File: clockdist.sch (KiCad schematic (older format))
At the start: 6 parts, among them U33 74LS258

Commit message: Fix some symbols
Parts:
- gave numbers to parts that had none: 1
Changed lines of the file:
@@
 U 1 1 5D89015C
 P 4050 2800
-F 0 "U33" H 4075 3125 50  0000 C CNN
-F 1 "74LS258" H 4075 3034 50  0000 C CNN
+F 0 "U33" H 4100 2950 50  0000 C CNN
+F 1 "74LS258" H 3750 2600 50  0000 C CNN
 F 2 "" H 4050 2800 50  0001 C CNN
 F 3 "http://www.ti.com/lit/gpn/sn74LS258" H 4050 2800 50  0001 C CNN
@@
 CCK
 $Comp
-L 74ls258:74LS258 U?
+L 74ls258:74LS258 U33
 U 2 1 5D895568
 P 4050 4200
-F 0 "U?" H 4075 4525 50  0000 C CNN
-F 1 "74LS258" H 4075 4434 50  0000 C CNN
+F 0 "U33" H 4100 4350 50  0000 C CNN
+F 1 "74LS258" H 3750 4000 50  0000 C CNN
 F 2 "" H 7150 1900 50  0001 C CNN
 F 3 "http://www.ti.com/lit/gpn/sn74LS258" H 7150 1900 50  0001 C CNN
@@
 $EndComp
 $Comp
-L 74ls258:74LS258 U?
+L 74ls258:74LS258 U33
 U 3 1 5D8955FE
 P 4050 3500
-F 0 "U?" H 4075 3825 50  0000 C CNN
-F 1 "74LS258" H 4075 3734 50  0000 C CNN
+F 0 "U33" H 4100 3650 50  0000 C CNN
+F 1 "74LS258" H 3750 3300 50  0000 C CNN
 F 2 "" H 7150 1200 50  0001 C CNN
 F 3 "http://www.ti.com/lit/gpn/sn74LS258" H 7150 1200 50  0001 C CNN
@@
 $EndComp
 $Comp
-L power:GND #PWR?
+L power:GND #PWR0202
 U 1 1 5D8A9F76
 P 8950 4200
-F 0 "#PWR?" H 8950 3950 50  0001 C CNN
+F 0 "#PWR0202" H 8950 3950 50  0001 C CNN
 F 1 "GND" H 8955 4027 50  0000 C CNN
 F 2 "" H 8950 4200 50  0001 C CNN
@@
 	8950 4200 8950 4050
 $Comp
-L power:VCC #PWR?
+L power:VCC #PWR0203
 U 1 1 5D8AA81C
 P 8950 2950
-F 0 "#PWR?" H 8950 2800 50  0001 C CNN
+F 0 "#PWR0203" H 8950 2800 50  0001 C CNN
 F 1 "VCC" H 8967 3123 50  0000 C CNN
 F 2 "" H 8950 2950 50  0001 C CNN
@@
 	4700 3000 4700 3700
 $Comp
-L power:GND #PWR?
+L power:GND #PWR0204
 U 1 1 5D8ABB37
 P 4700 4850
-F 0 "#PWR?" H 4700 4600 50  0001 C CNN
+F 0 "#PWR0204" H 4700 4600 50  0001 C CNN
 F 1 "GND" H 4705 4677 50  0000 C CNN
 F 2 "" H 4700 4850 50  0001 C CNN

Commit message: Add video power
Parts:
- RP103: footprint (none) -> Resistor_THT:R_Array_SIP10
- U33: footprint (none) -> Package_DIP:DIP-16_W7.62mm_Socket_LongPads
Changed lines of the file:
@@
 F 0 "U33" H 4100 2950 50  0000 C CNN
 F 1 "74LS258" H 3750 2600 50  0000 C CNN
-F 2 "" H 4050 2800 50  0001 C CNN
+F 2 "Package_DIP:DIP-16_W7.62mm_Socket_LongPads" H 4050 2800 50  0001 C CNN
 F 3 "http://www.ti.com/lit/gpn/sn74LS258" H 4050 2800 50  0001 C CNN
 	1    4050 2800
@@
 F 0 "U33" H 4100 4350 50  0000 C CNN
 F 1 "74LS258" H 3750 4000 50  0000 C CNN
-F 2 "" H 7150 1900 50  0001 C CNN
+F 2 "Package_DIP:DIP-16_W7.62mm_Socket_LongPads" H 7150 1900 50  0001 C CNN
 F 3 "http://www.ti.com/lit/gpn/sn74LS258" H 7150 1900 50  0001 C CNN
 	2    4050 4200
@@
 F 0 "U33" H 4100 3650 50  0000 C CNN
 F 1 "74LS258" H 3750 3300 50  0000 C CNN
-F 2 "" H 7150 1200 50  0001 C CNN
+F 2 "Package_DIP:DIP-16_W7.62mm_Socket_LongPads" H 7150 1200 50  0001 C CNN
 F 3 "http://www.ti.com/lit/gpn/sn74LS258" H 7150 1200 50  0001 C CNN
 	3    4050 3500
@@
 F 0 "RP103" V 5233 3500 50  0000 C CNN
 F 1 "39" V 5324 3500 50  0000 C CNN
-F 2 "" V 6025 3500 50  0001 C CNN
+F 2 "Resistor_THT:R_Array_SIP10" V 6025 3500 50  0001 C CNN
 F 3 "~" H 5650 3500 50  0001 C CNN
 	1    5650 3500
@@
 F 0 "U33" H 9180 3671 50  0000 L CNN
 F 1 "74LS258" H 9180 3580 50  0000 L CNN
-F 2 "" H 12050 1300 50  0001 C CNN
+F 2 "Package_DIP:DIP-16_W7.62mm_Socket_LongPads" H 12050 1300 50  0001 C CNN
 F 3 "http://www.ti.com/lit/gpn/sn74LS258" H 12050 1300 50  0001 C CNN
 	5    8950 3600

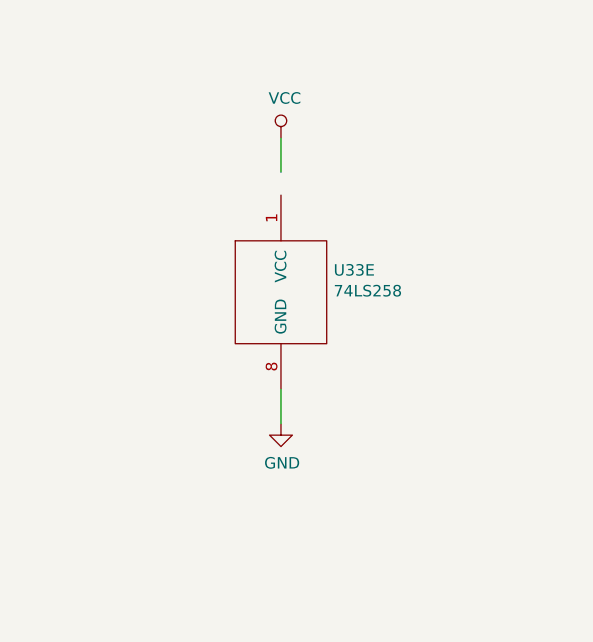
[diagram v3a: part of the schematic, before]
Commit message: Add power & decoupling, not yet complete
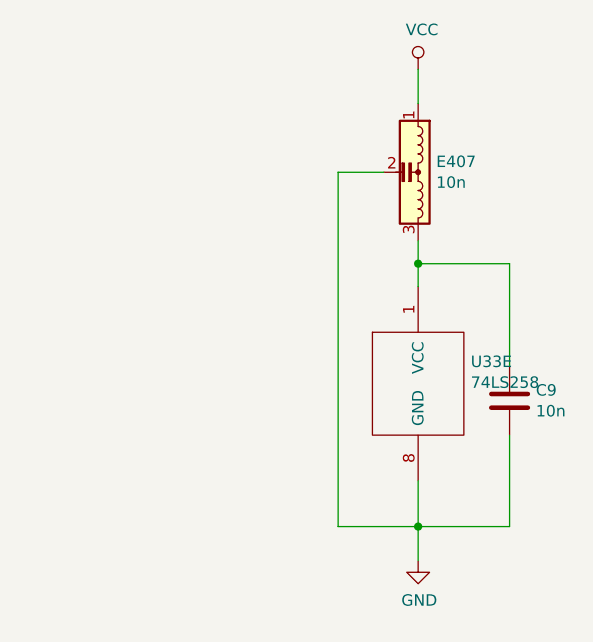
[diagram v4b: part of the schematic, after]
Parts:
- added C9: 10n, symbol Device:C
- added E407: 10n, symbol emi_filter_lcl_small:EMI_Filter_LCL
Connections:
- net GND: now also C9.2, E407.2
- net VCC: now also E407.1
- net at U33.1 (VCC): now also C9.1, E407.3
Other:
- moved on the sheet: U33E
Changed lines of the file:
@@
 $Descr A4 11693 8268
 encoding utf-8
-Sheet 10 11
+Sheet 10 12
 Title "Rämixx500"
 Date "2019-04-20"
@@
 L 74ls258:74LS258 U33
 U 5 1 5D8A9E7D
-P 8950 3600
-F 0 "U33" H 9180 3671 50  0000 L CNN
-F 1 "74LS258" H 9180 3580 50  0000 L CNN
-F 2 "Package_DIP:DIP-16_W7.62mm_Socket_LongPads" H 12050 1300 50  0001 C CNN
-F 3 "http://www.ti.com/lit/gpn/sn74LS258" H 12050 1300 50  0001 C CNN
-	5    8950 3600
+P 9550 4000
+F 0 "U33" H 9780 4071 50  0000 L CNN
+F 1 "74LS258" H 9780 3980 50  0000 L CNN
+F 2 "Package_DIP:DIP-16_W7.62mm_Socket_LongPads" H 12650 1700 50  0001 C CNN
+F 3 "http://www.ti.com/lit/gpn/sn74LS258" H 12650 1700 50  0001 C CNN
+	5    9550 4000
 	1    0    0    -1
 $EndComp
@@
 L power:GND #PWR0202
 U 1 1 5D8A9F76
-P 8950 4200
-F 0 "#PWR0202" H 8950 3950 50  0001 C CNN
-F 1 "GND" H 8955 4027 50  0000 C CNN
-F 2 "" H 8950 4200 50  0001 C CNN
-F 3 "" H 8950 4200 50  0001 C CNN
-	1    8950 4200
-	1    0    0    -1
-$EndComp
-Wire Wire Line
-	8950 4200 8950 4050
+P 9550 4800
+F 0 "#PWR0202" H 9550 4550 50  0001 C CNN
+F 1 "GND" H 9555 4627 50  0000 C CNN
+F 2 "" H 9550 4800 50  0001 C CNN
+F 3 "" H 9550 4800 50  0001 C CNN
+	1    9550 4800
+	1    0    0    -1
+$EndComp
+Wire Wire Line
+	9550 4800 9550 4650
 $Comp
 L power:VCC #PWR0203
 U 1 1 5D8AA81C
-P 8950 2950
-F 0 "#PWR0203" H 8950 2800 50  0001 C CNN
-F 1 "VCC" H 8967 3123 50  0000 C CNN
-F 2 "" H 8950 2950 50  0001 C CNN
-F 3 "" H 8950 2950 50  0001 C CNN
-	1    8950 2950
-	1    0    0    -1
-$EndComp
-Wire Wire Line
-	8950 2950 8950 3100
+P 9550 2650
+F 0 "#PWR0203" H 9550 2500 50  0001 C CNN
+F 1 "VCC" H 9567 2823 50  0000 C CNN
+F 2 "" H 9550 2650 50  0001 C CNN
+F 3 "" H 9550 2650 50  0001 C CNN
+	1    9550 2650
+	1    0    0    -1
+$EndComp
+Wire Wire Line
+	9550 2650 9550 2800
 Wire Wire Line
 	4200 2950 4200 3000
@@
 Wire Wire Line
 	4700 4400 4700 4850
+$Comp
+L emi_filter_lcl_small:EMI_Filter_LCL E?
+U 1 1 5EFD7951
+P 9450 3100
+AR Path="/5E9E4C57/5EFD7951" Ref="E?"  Part="1"
+AR Path="/5D88EC26/5EFD7951" Ref="E407"  Part="1"
+F 0 "E407" V 9404 3279 50  0000 L CNN
+F 1 "10n" V 9495 3279 50  0000 L CNN
+F 2 "" V 9450 3100 50  0001 C CNN
+F 3 "http://www.murata.com/~/media/webrenewal/support/library/catalog/products/emc/emifil/c31e.ashx?la=en-gb" V 9450 3100 50  0001 C CNN
+	1    9450 3100
+	0    1    1    0
+$EndComp
+Wire Wire Line
+	9400 3100 9200 3100
+Wire Wire Line
+	9200 3100 9200 4650
+Wire Wire Line
+	9200 4650 9550 4650
+Wire Wire Line
+	9550 4450 9550 4650
+Connection ~ 9550 4650
+Wire Wire Line
+	9550 4650 9950 4650
+Wire Wire Line
+	9950 4250 9950 4650
+$Comp
+L Device:C C?
+U 1 1 5EFD7963
+P 9950 4100
+AR Path="/5E9E4C57/5EFD7963" Ref="C?"  Part="1"
+AR Path="/5D88EC26/5EFD7963" Ref="C9"  Part="1"
+F 0 "C9" H 10065 4146 50  0000 L CNN
+F 1 "10n" H 10065 4055 50  0000 L CNN
+F 2 "" H 9988 3950 50  0001 C CNN
+F 3 "~" H 9950 4100 50  0001 C CNN
+	1    9950 4100
+	1    0    0    -1
+$EndComp
+Wire Wire Line
+	9950 3500 9950 3950
+Wire Wire Line
+	9550 3600 9550 3500
+Wire Wire Line
+	9550 3400 9550 3500
+Connection ~ 9550 3500
+Wire Wire Line
+	9550 3500 9950 3500
 $EndSCHEMATC

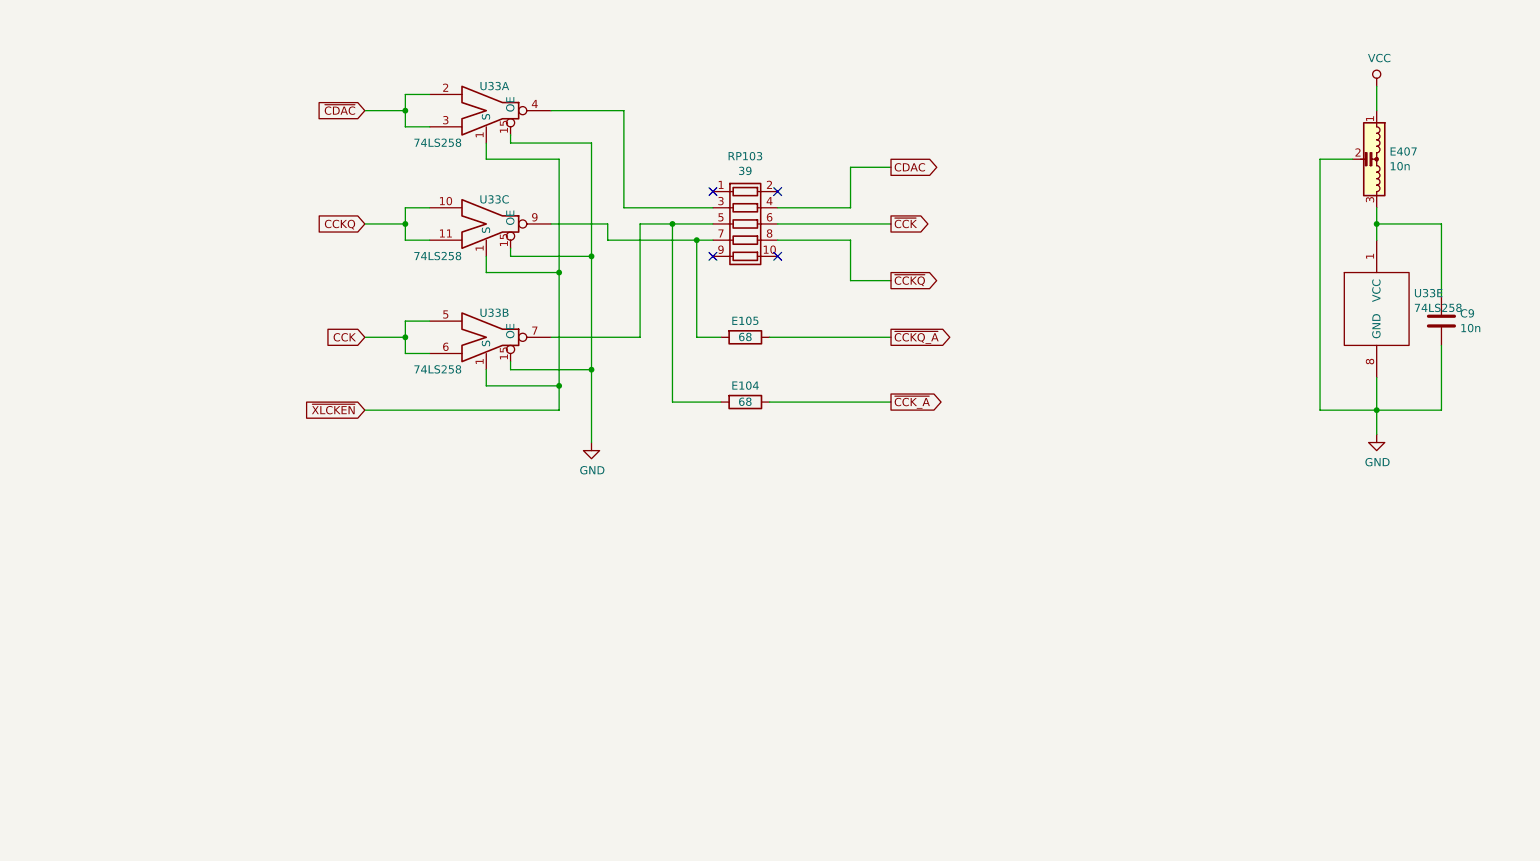
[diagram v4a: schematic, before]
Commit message: Add power input and complete clock distribution
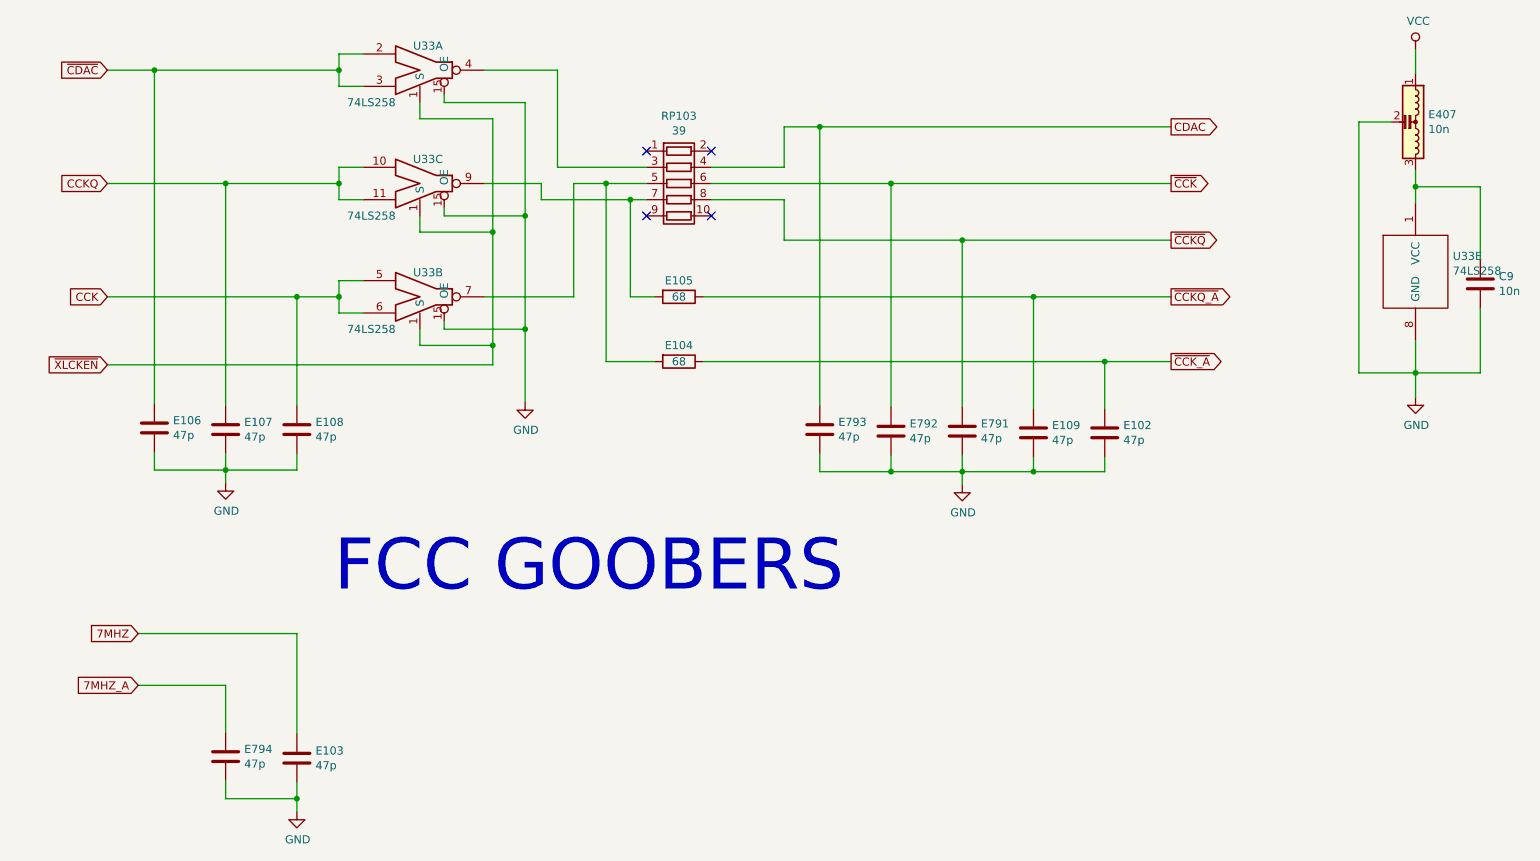
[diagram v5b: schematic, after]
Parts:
- added E102, E103, E106, E107, E108, E109, E791, E792, E793, E794: 47p, symbol Device:C
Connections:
- net CCK: now also E108.1
- net CCKQ: now also E107.1
- net CDAC: now also E793.1
- net GND: now also E102.2, E103.2, E106.2, E107.2, E108.2, E109.2, E791.2, E792.2, E793.2, E794.2
- net ~CCK: now also E792.1
- net ~CCKQ: now also E791.1
- net ~CCKQ_A: now also E109.1
- net ~CCK_A: now also E102.1
- net ~CDAC: now also E106.1
- new net 7MHZ: E103.1
- new net 7MHZ_A: E794.1
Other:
- note added: "FCC GOOBERS"
- moved on the sheet: C9, E104, E105, E407, RP103, U33A, U33B, U33C, U33E

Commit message: Add RTC
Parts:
- renumbered C9 to C33
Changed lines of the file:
@@
 $Descr A4 11693 8268
 encoding utf-8
-Sheet 10 12
+Sheet 10 13
 Title "Rämixx500"
 Date "2019-04-20"
@@
 U 5 1 5D8A9E7D
 P 9790 3770
-F 0 "U33" H 10020 3841 50  0000 L CNN
-F 1 "74LS258" H 10020 3750 50  0000 L CNN
+F 0 "U33" H 9870 4030 50  0000 L CNN
+F 1 "74LS258" H 9830 3450 50  0000 L CNN
 F 2 "Package_DIP:DIP-16_W7.62mm_Socket_LongPads" H 12890 1470 50  0001 C CNN
 F 3 "http://www.ti.com/lit/gpn/sn74LS258" H 12890 1470 50  0001 C CNN
@@
 P 10190 3870
 AR Path="/5E9E4C57/5EFD7963" Ref="C?"  Part="1"
-AR Path="/5D88EC26/5EFD7963" Ref="C9"  Part="1"
-F 0 "C9" H 10305 3916 50  0000 L CNN
+AR Path="/5D88EC26/5EFD7963" Ref="C33"  Part="1"
+F 0 "C33" H 10305 3916 50  0000 L CNN
 F 1 "10n" H 10305 3825 50  0000 L CNN
 F 2 "" H 10228 3720 50  0001 C CNN
@@
 	2440 5020 2440 5100
 $Comp
-L power:GND #PWR?
+L power:GND #PWR0238
 U 1 1 5CF1173C
 P 2440 5100
-F 0 "#PWR?" H 2440 4850 50  0001 C CNN
+F 0 "#PWR0238" H 2440 4850 50  0001 C CNN
 F 1 "GND" H 2445 4927 50  0000 C CNN
 F 2 "" H 2440 5100 50  0001 C CNN
@@
 	6990 5030 6990 5110
 $Comp
-L power:GND #PWR?
+L power:GND #PWR0239
 U 1 1 5CF1188B
 P 6990 5110
-F 0 "#PWR?" H 6990 4860 50  0001 C CNN
+F 0 "#PWR0239" H 6990 4860 50  0001 C CNN
 F 1 "GND" H 6995 4937 50  0000 C CNN
 F 2 "" H 6990 5110 50  0001 C CNN
@@
 	2880 7050 2880 7130
 $Comp
-L power:GND #PWR?
+L power:GND #PWR0240
 U 1 1 5CF1A8EC
 P 2880 7130
-F 0 "#PWR?" H 2880 6880 50  0001 C CNN
+F 0 "#PWR0240" H 2880 6880 50  0001 C CNN
 F 1 "GND" H 2885 6957 50  0000 C CNN
 F 2 "" H 2880 7130 50  0001 C CNN

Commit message: Fix power-up reset
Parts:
- E102, E103, E106, E107, E108: footprint (none) -> Raemixx500:C_Axial_L9.0mm_D3.2mm_P12.70mm
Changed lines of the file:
@@
 EESchema Schematic File Version 4
 LIBS:Raemix500-cache
-EELAYER 26 0
+EELAYER 29 0
 EELAYER END
 $Descr A4 11693 8268
@@
 F 0 "E102" H 7985 4836 50  0000 L CNN
 F 1 "47p" H 7985 4745 50  0000 L CNN
-F 2 "" H 7908 4640 50  0001 C CNN
+F 2 "Raemixx500:C_Axial_L9.0mm_D3.2mm_P12.70mm" H 7908 4640 50  0001 C CNN
 F 3 "~" H 7870 4790 50  0001 C CNN
 	1    7870 4790
@@
 F 0 "E106" H 2115 4806 50  0000 L CNN
 F 1 "47p" H 2115 4715 50  0000 L CNN
-F 2 "" H 2038 4610 50  0001 C CNN
+F 2 "Raemixx500:C_Axial_L9.0mm_D3.2mm_P12.70mm" H 2038 4610 50  0001 C CNN
 F 3 "~" H 2000 4760 50  0001 C CNN
 	1    2000 4760
@@
 F 0 "E107" H 2555 4816 50  0000 L CNN
 F 1 "47p" H 2555 4725 50  0000 L CNN
-F 2 "" H 2478 4620 50  0001 C CNN
+F 2 "Raemixx500:C_Axial_L9.0mm_D3.2mm_P12.70mm" H 2478 4620 50  0001 C CNN
 F 3 "~" H 2440 4770 50  0001 C CNN
 	1    2440 4770
@@
 F 0 "E108" H 2995 4816 50  0000 L CNN
 F 1 "47p" H 2995 4725 50  0000 L CNN
-F 2 "" H 2918 4620 50  0001 C CNN
+F 2 "Raemixx500:C_Axial_L9.0mm_D3.2mm_P12.70mm" H 2918 4620 50  0001 C CNN
 F 3 "~" H 2880 4770 50  0001 C CNN
 	1    2880 4770
@@
 F 0 "E103" H 2995 6846 50  0000 L CNN
 F 1 "47p" H 2995 6755 50  0000 L CNN
-F 2 "" H 2918 6650 50  0001 C CNN
+F 2 "Raemixx500:C_Axial_L9.0mm_D3.2mm_P12.70mm" H 2918 6650 50  0001 C CNN
 F 3 "~" H 2880 6800 50  0001 C CNN
 	1    2880 6800
